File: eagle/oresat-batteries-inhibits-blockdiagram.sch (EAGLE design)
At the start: 7 parts

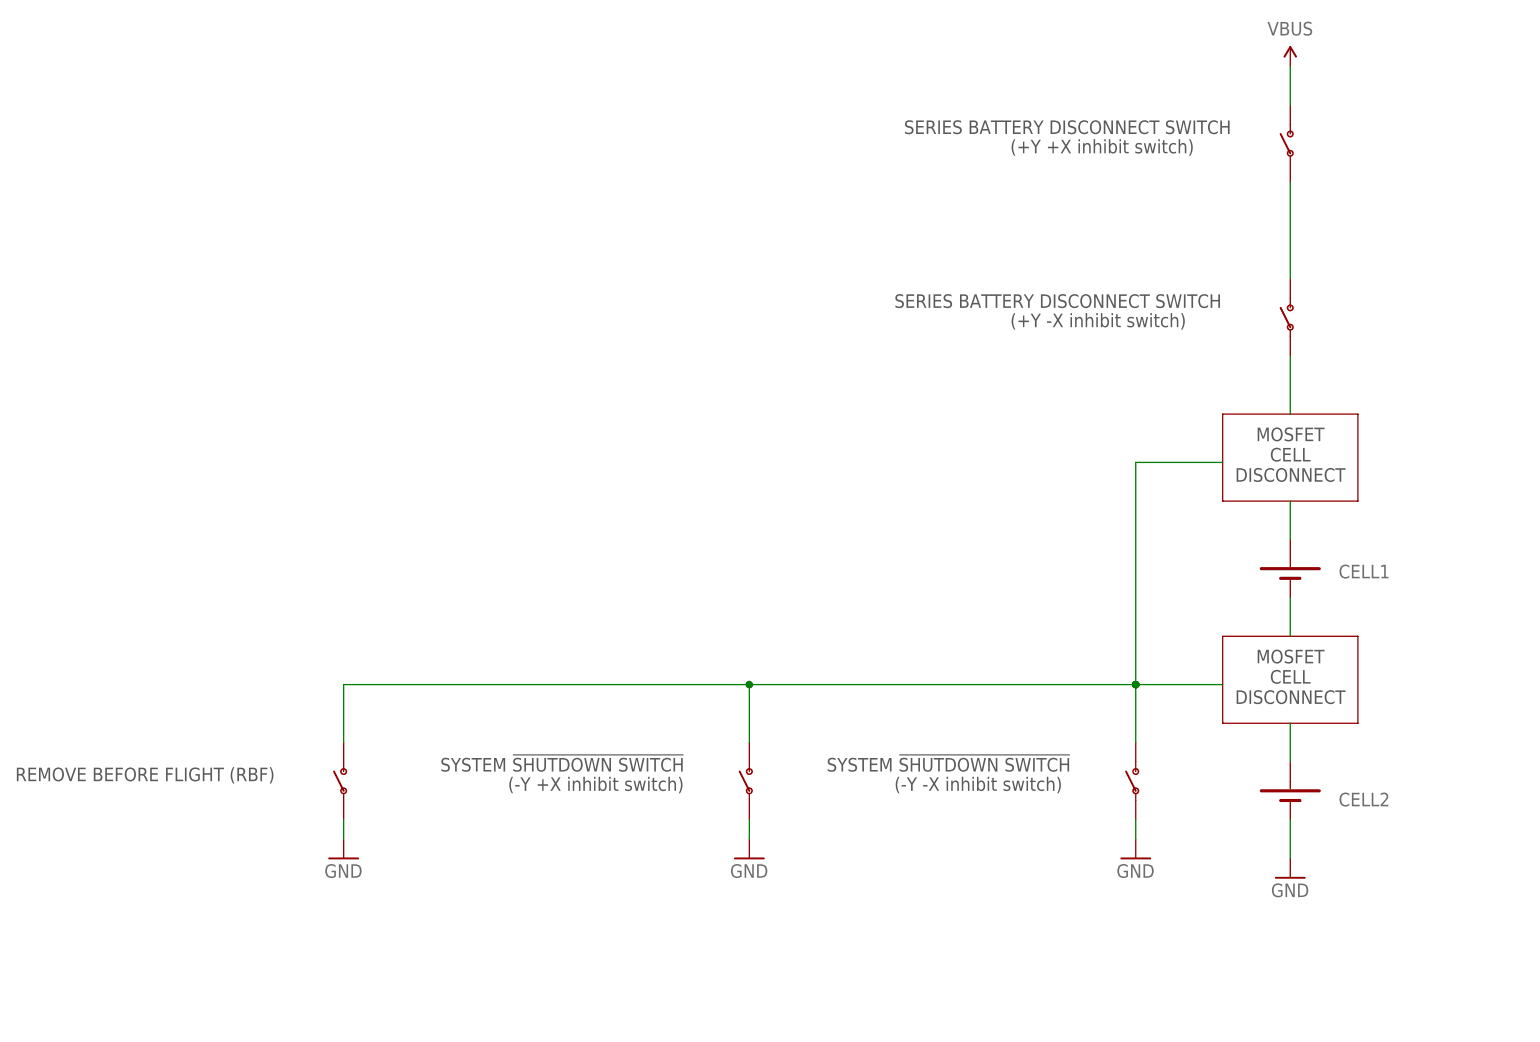
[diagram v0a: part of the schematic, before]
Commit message: Updated inhibit switch diagram to be more compact, reflect Nanoracks SDT call outs
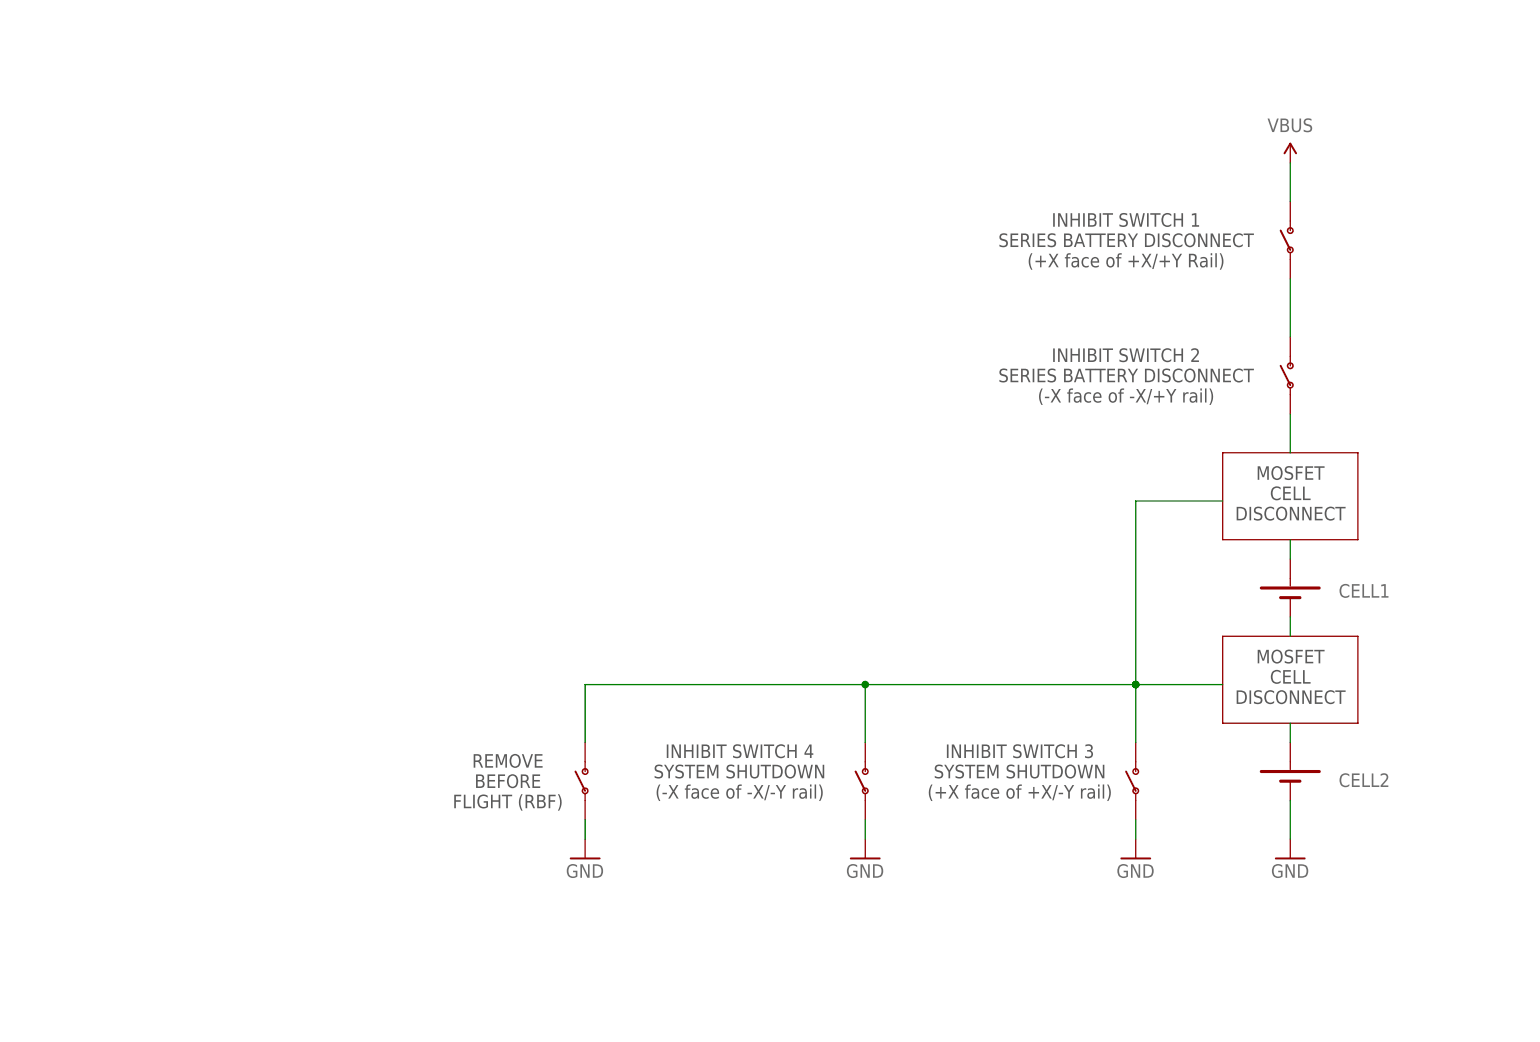
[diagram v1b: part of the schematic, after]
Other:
- note added: "INHIBIT SWITCH 1 SERIES BATTERY DISCONNECT (+X face of +X/+Y Rail)"
- note added: "INHIBIT SWITCH 2 SERIES BATTERY DISCONNECT (-X face of -X/+Y rail)"
- note added: "INHIBIT SWITCH 3 SYSTEM SHUTDOWN (+X face of +X/-Y rail)"
- note added: "INHIBIT SWITCH 4 SYSTEM SHUTDOWN (-X face of -X/-Y rail)"
- note removed: "(+Y +X inhibit switch)"
- note removed: "(+Y -X inhibit switch)"
- note removed: "(-Y +X inhibit switch)"
- note removed: "(-Y -X inhibit switch)"
- note removed: "SERIES BATTERY DISCONNECT SWITCH"
- note removed: "SYSTEM !SHUTDOWN SWITCH"
- moved on the sheet: CELL1, CELL2
